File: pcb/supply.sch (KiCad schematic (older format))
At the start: 11 parts, among them J1 Barrel_Jack_Switch, J13 Conn_01x02_Female, U9 ZLDO1117G33TA

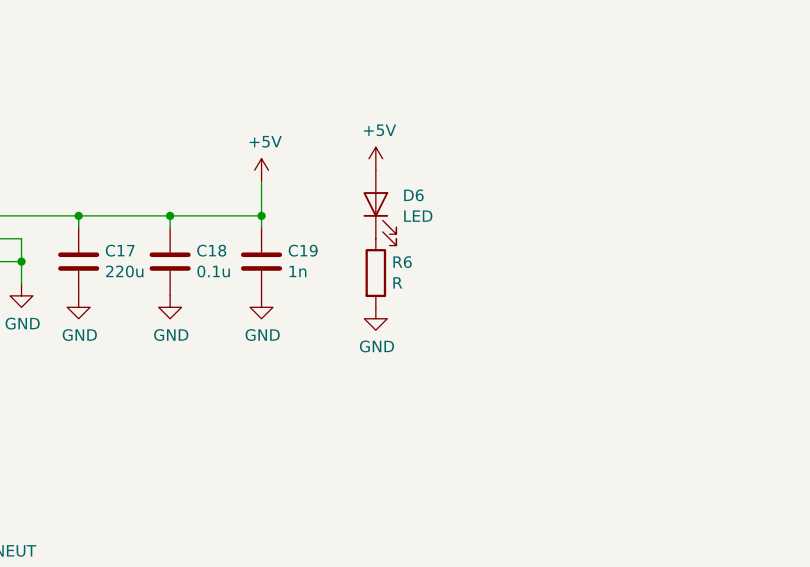
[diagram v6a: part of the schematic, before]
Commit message: added footprints in supply sheet
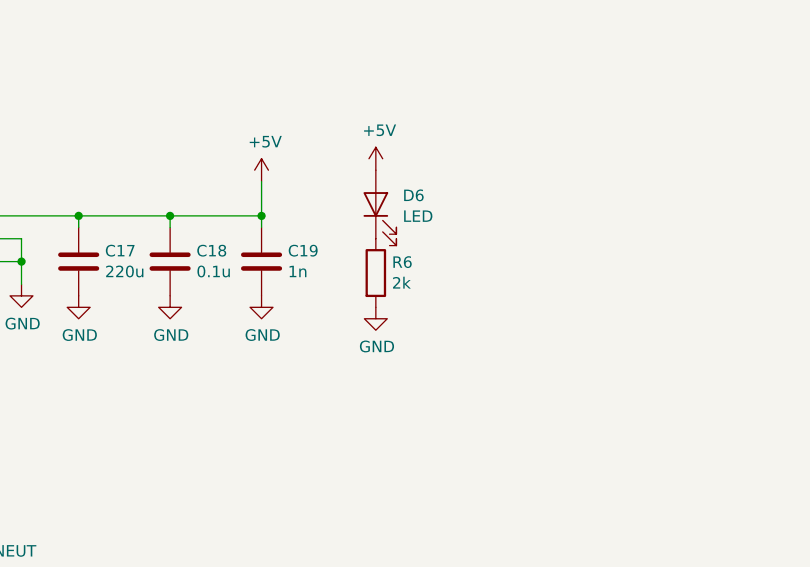
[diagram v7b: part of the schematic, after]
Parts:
- C16, C21: footprint (none) -> Capacitor_SMD:C_1206_3216Metric; DigiKey (none) -> 445-14751-1-ND
- C18, C20: footprint (none) -> Capacitor_SMD:C_0603_1608Metric; DigiKey (none) -> 720-1688-1-ND
- C19: footprint (none) -> Capacitor_SMD:C_0603_1608Metric; DigiKey (none) -> 399-17840-1-ND
- D6: footprint (none) -> LED_SMD:LED_0805_2012Metric; DigiKey (none) -> 732-4983-1-ND
- J1: DigiKey (none) -> CP-002A-ND
- R6: value R -> 2k; footprint (none) -> Resistor_SMD:R_0603_1608Metric
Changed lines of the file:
@@
 EESchema Schematic File Version 4
-LIBS:keep_breathing_ctrl-cache
 EELAYER 30 0
 EELAYER END
@@
 F 2 "TH:BARREL_JACK" H 1750 1910 50  0001 C CNN
 F 3 "~" H 1750 1910 50  0001 C CNN
+F 4 "CP-002A-ND" H 1700 1950 50  0001 C CNN "DigiKey"
 	1    1700 1950
 	1    0    0    -1
@@
 F 0 "C18" H 2965 2096 50  0000 L CNN
 F 1 "0.1u" H 2965 2005 50  0000 L CNN
-F 2 "" H 2888 1900 50  0001 C CNN
+F 2 "Capacitor_SMD:C_0603_1608Metric" H 2888 1900 50  0001 C CNN
 F 3 "~" H 2850 2050 50  0001 C CNN
+F 4 "720-1688-1-ND" H 2850 2050 50  0001 C CNN "DigiKey"
 	1    2850 2050
 	1    0    0    -1
@@
 F 0 "C19" H 3365 2096 50  0000 L CNN
 F 1 "1n" H 3365 2005 50  0000 L CNN
-F 2 "" H 3288 1900 50  0001 C CNN
+F 2 "Capacitor_SMD:C_0603_1608Metric" H 3288 1900 50  0001 C CNN
 F 3 "~" H 3250 2050 50  0001 C CNN
+F 4 "399-17840-1-ND" H 3250 2050 50  0001 C CNN "DigiKey"
 	1    3250 2050
 	1    0    0    -1
@@
 F 0 "D6" V 3788 1683 50  0000 R CNN
 F 1 "LED" V 3697 1683 50  0000 R CNN
-F 2 "" H 3750 1800 50  0001 C CNN
+F 2 "LED_SMD:LED_0805_2012Metric" H 3750 1800 50  0001 C CNN
 F 3 "~" H 3750 1800 50  0001 C CNN
+F 4 "732-4983-1-ND" V 3750 1800 50  0001 C CNN "DigiKey"
 	1    3750 1800
 	0    -1   -1   0
@@
 P 3750 2100
 F 0 "R6" H 3820 2146 50  0000 L CNN
-F 1 "R" H 3820 2055 50  0000 L CNN
-F 2 "" V 3680 2100 50  0001 C CNN
+F 1 "2k" H 3820 2055 50  0000 L CNN
+F 2 "Resistor_SMD:R_0603_1608Metric" V 3680 2100 50  0001 C CNN
 F 3 "~" H 3750 2100 50  0001 C CNN
 	1    3750 2100
@@
 F 0 "C20" H 9465 1596 50  0000 L CNN
 F 1 "0.1u" H 9465 1505 50  0000 L CNN
-F 2 "" H 9388 1400 50  0001 C CNN
+F 2 "Capacitor_SMD:C_0603_1608Metric" H 9388 1400 50  0001 C CNN
 F 3 "~" H 9350 1550 50  0001 C CNN
+F 4 "720-1688-1-ND" H 9350 1550 50  0001 C CNN "DigiKey"
 	1    9350 1550
 	1    0    0    -1
@@
 F 0 "C21" H 9865 1596 50  0000 L CNN
 F 1 "33u" H 9865 1505 50  0000 L CNN
-F 2 "" H 9788 1400 50  0001 C CNN
+F 2 "Capacitor_SMD:C_1206_3216Metric" H 9788 1400 50  0001 C CNN
 F 3 "~" H 9750 1550 50  0001 C CNN
+F 4 "445-14751-1-ND" H 9750 1550 50  0001 C CNN "DigiKey"
 	1    9750 1550
 	1    0    0    -1
@@
 F 0 "C16" H 7565 1696 50  0000 L CNN
 F 1 "33u" H 7565 1605 50  0000 L CNN
-F 2 "" H 7488 1500 50  0001 C CNN
+F 2 "Capacitor_SMD:C_1206_3216Metric" H 7488 1500 50  0001 C CNN
 F 3 "~" H 7450 1650 50  0001 C CNN
+F 4 "445-14751-1-ND" H 7450 1650 50  0001 C CNN "DigiKey"
 	1    7450 1650
 	1    0    0    -1

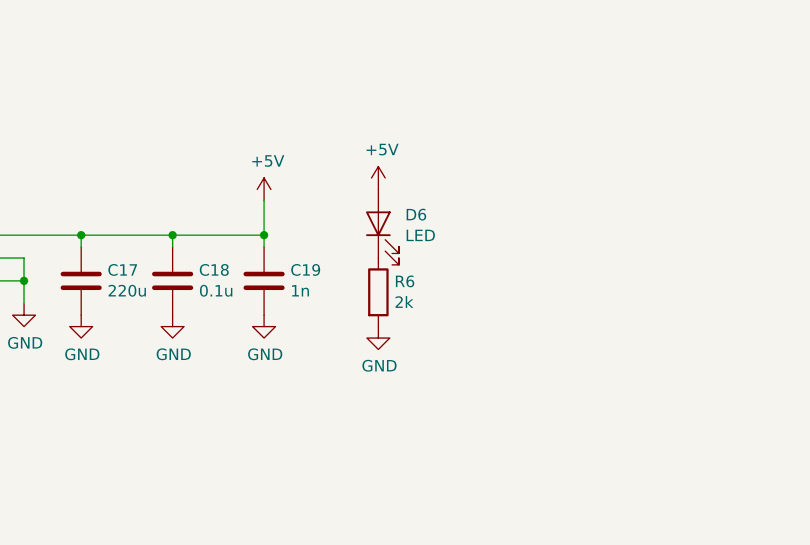
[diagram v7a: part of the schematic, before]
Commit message: Connections in the schema were modified and components some components from supply and electrovalves were positioned on the PCB
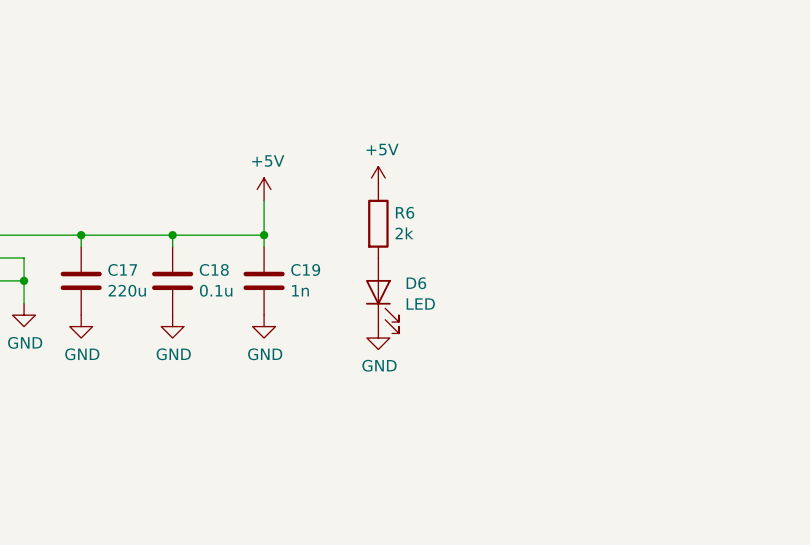
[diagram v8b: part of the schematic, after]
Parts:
- C17: footprint (none) -> Capacitor_SMD:C_1206_3216Metric; DIgiKey (none) -> 490-13250-1-ND
- R6: footprint Resistor_SMD:R_0603_1608Metric -> Resistor_SMD:R_0402_1005Metric
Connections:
- net +5V: now also R6.1; no longer D6.2 (A)
- net GND: now also D6.1 (K); no longer R6.2
- new net: D6.2 (A), R6.2
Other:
- moved on the sheet: D6, R6
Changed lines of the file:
@@
 F 0 "C17" H 2565 2096 50  0000 L CNN
 F 1 "220u" H 2565 2005 50  0000 L CNN
-F 2 "" H 2488 1900 50  0001 C CNN
+F 2 "Capacitor_SMD:C_1206_3216Metric" H 2488 1900 50  0001 C CNN
 F 3 "~" H 2450 2050 50  0001 C CNN
+F 4 "490-13250-1-ND" H 2450 2050 50  0001 C CNN "DIgiKey"
 	1    2450 2050
 	1    0    0    -1
@@
 L Device:LED D6
 U 1 1 5E9039A0
-P 3750 1800
-F 0 "D6" V 3788 1683 50  0000 R CNN
-F 1 "LED" V 3697 1683 50  0000 R CNN
-F 2 "LED_SMD:LED_0805_2012Metric" H 3750 1800 50  0001 C CNN
-F 3 "~" H 3750 1800 50  0001 C CNN
-F 4 "732-4983-1-ND" V 3750 1800 50  0001 C CNN "DigiKey"
-	1    3750 1800
+P 3750 2100
+F 0 "D6" V 3788 1983 50  0000 R CNN
+F 1 "LED" V 3697 1983 50  0000 R CNN
+F 2 "LED_SMD:LED_0805_2012Metric" H 3750 2100 50  0001 C CNN
+F 3 "~" H 3750 2100 50  0001 C CNN
+F 4 "732-4983-1-ND" V 3750 2100 50  0001 C CNN "DigiKey"
+	1    3750 2100
 	0    -1   -1   0
 $EndComp
@@
 L Device:R R6
 U 1 1 5E903B44
-P 3750 2100
-F 0 "R6" H 3820 2146 50  0000 L CNN
-F 1 "2k" H 3820 2055 50  0000 L CNN
-F 2 "Resistor_SMD:R_0603_1608Metric" V 3680 2100 50  0001 C CNN
-F 3 "~" H 3750 2100 50  0001 C CNN
-	1    3750 2100
+P 3750 1800
+F 0 "R6" H 3820 1846 50  0000 L CNN
+F 1 "2k" H 3820 1755 50  0000 L CNN
+F 2 "Resistor_SMD:R_0402_1005Metric" V 3680 1800 50  0001 C CNN
+F 3 "~" H 3750 1800 50  0001 C CNN
+	1    3750 1800
 	1    0    0    -1
 $EndComp
